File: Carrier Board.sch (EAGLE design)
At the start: 65 parts, among them J1 H4P-SMD-2.0, J2 H4P-SMD-2.0, J3 H4P-SMD-2.0, J5 S2B-PH-SM4-TB(LF)(SN), J6 S2B-PH-SM4-TB(LF)(SN), P1 PARTICLE-DEVICES-BORON, Q1 BSS138, Q2 BSS138, SW1 MF-SW-TACT-6MM, U1 TMP36GRTZ, U2 MB85RC64, U3 TPL5010, U4 TPS22810, U5 TPS22810, U7 NL17SZ74USG, U8 MCP79410T-I/SN, Y1 ECS-.327-6-17X-TR

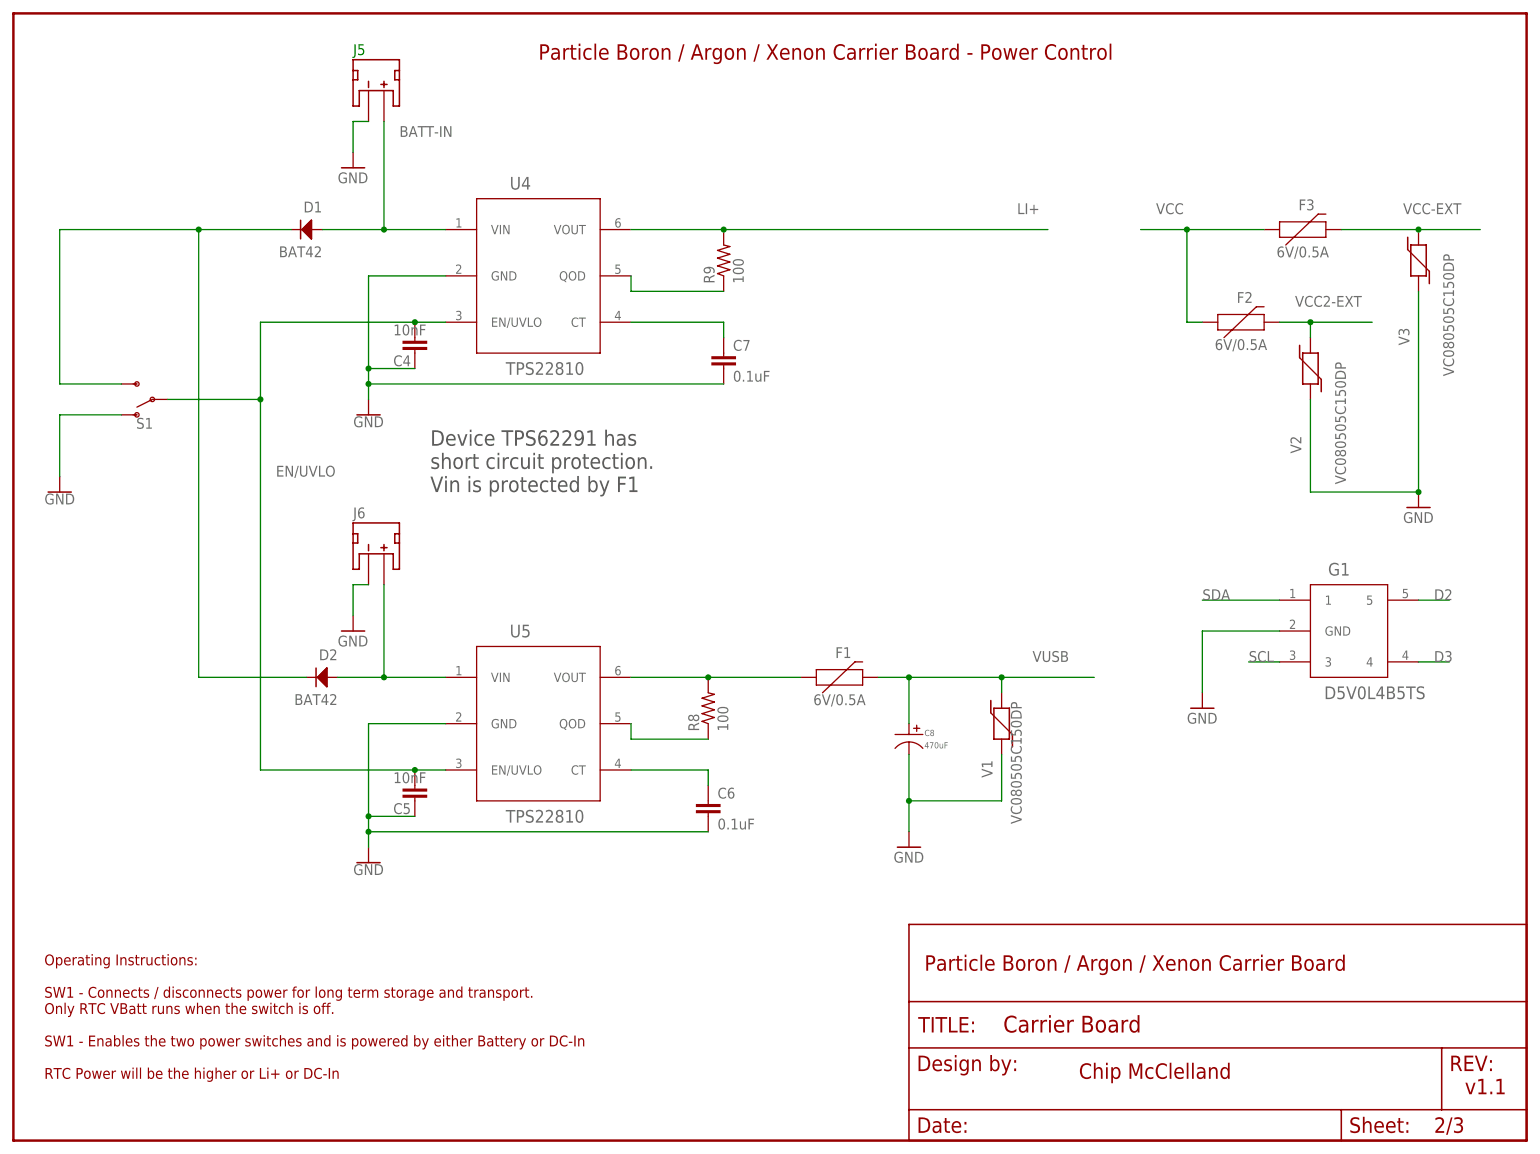
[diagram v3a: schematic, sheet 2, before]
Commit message: Added Zener protection for Argon / Xenon
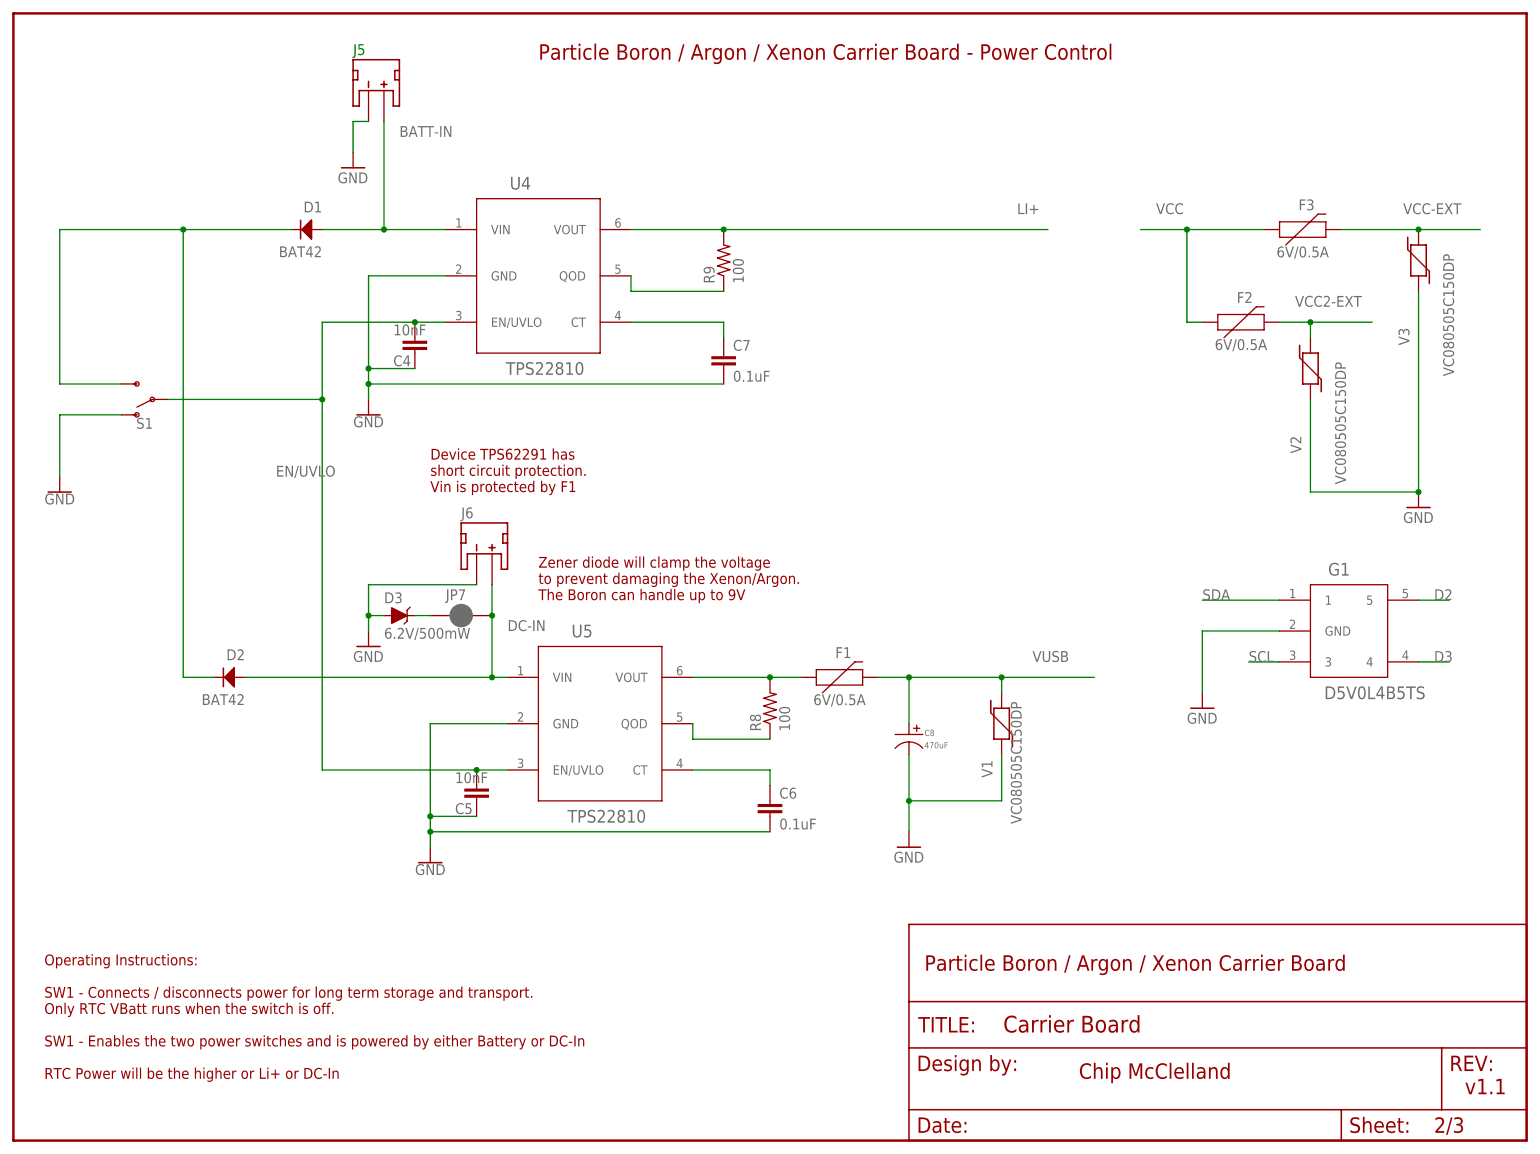
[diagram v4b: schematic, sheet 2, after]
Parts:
- added D3: 6.2V/500mW, SparkFun-DiscreteSemi:DIODE-ZENER-DZ2J150M0L
- added JP7: JUMPER-SMT_2_NC_PASTE_SILK, SparkFun-Jumpers:JUMPER-SMT_2_NC_PASTE_SILK
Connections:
- removed net N$11: D2.ANODE, J6.+, U5.VIN
- new net DC-IN: D2.ANODE, J6.+, JP7.1, U5.VIN
- new net N$1: D3.C, JP7.2
- net GND: now also D3.A
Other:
- note added: "Zener diode will clamp the voltage to prevent damaging the Xenon/Argon. The Boron can handle up to 9V"
- moved on the sheet: C5, C6, D2, J6, R8, U5

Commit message: Final Tweaks before MacroFab
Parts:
- F1: value 6V/0.5A -> 63V/1.5A
- H1, H2, H3, H4: POPULATE (none) -> 0
- J2: value H4P-SMD-2.0 -> (none); device OPL_Connector:GROVE-CONNECTOR-SMD(4+2P-2.0) -> SparkFun-Connectors:CONN_03X22X3_SILK_MALE_PTH; MPN B4B-PH-SM4-TB(LF)(SN) -> (none); POPULATE 1 -> 0
- J4: value (none) -> S2B-PH-SM4-TB(LF)(SN); device SparkFun-Connectors:CONN_03X22X3_SILK_MALE_PTH -> SparkFun-Connectors:JST_2MM_MALE; MFG (none) -> JST S2B-PH-SM4-TB(LF)(SN); POPULATE 0 -> (none)
- J6: value S2B-PH-SM4-TB(LF)(SN) -> H4P-SMD-2.0; device SparkFun-Connectors:JST_2MM_MALE -> OPL_Connector:GROVE-CONNECTOR-SMD(4+2P-2.0); MFG JST S2B-PH-SM4-TB(LF)(SN) -> (none); MPN (none) -> B4B-PH-SM4-TB(LF)(SN); POPULATE (none) -> 1
- renumbered JP2 to J7
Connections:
- net DC-IN: now also J4.+; no longer J6.+
- net GND: now also J2.1, J4.-, J6.4, J6.SS1, J6.SS2; no longer J2.4, J2.SS1, J2.SS2, J4.1, J6.-
- net MISO: now also J2.3; no longer J4.3
- net MOSI: now also J2.6; no longer J4.6
- net SCK: now also J2.4; no longer J4.4
- net SCL: now also J6.1; no longer J2.1
- net SDA: now also J6.2; no longer J2.2
- net SS: now also J2.2; no longer J4.2
- net VCC-EXT: now also J2.5; no longer J4.5
- net VCC2-EXT: now also J6.3; no longer J2.3
